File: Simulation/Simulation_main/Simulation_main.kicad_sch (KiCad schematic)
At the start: 13 parts, among them U1 ${SIM.PARAMS}, U2 ${SIM.PARAMS}

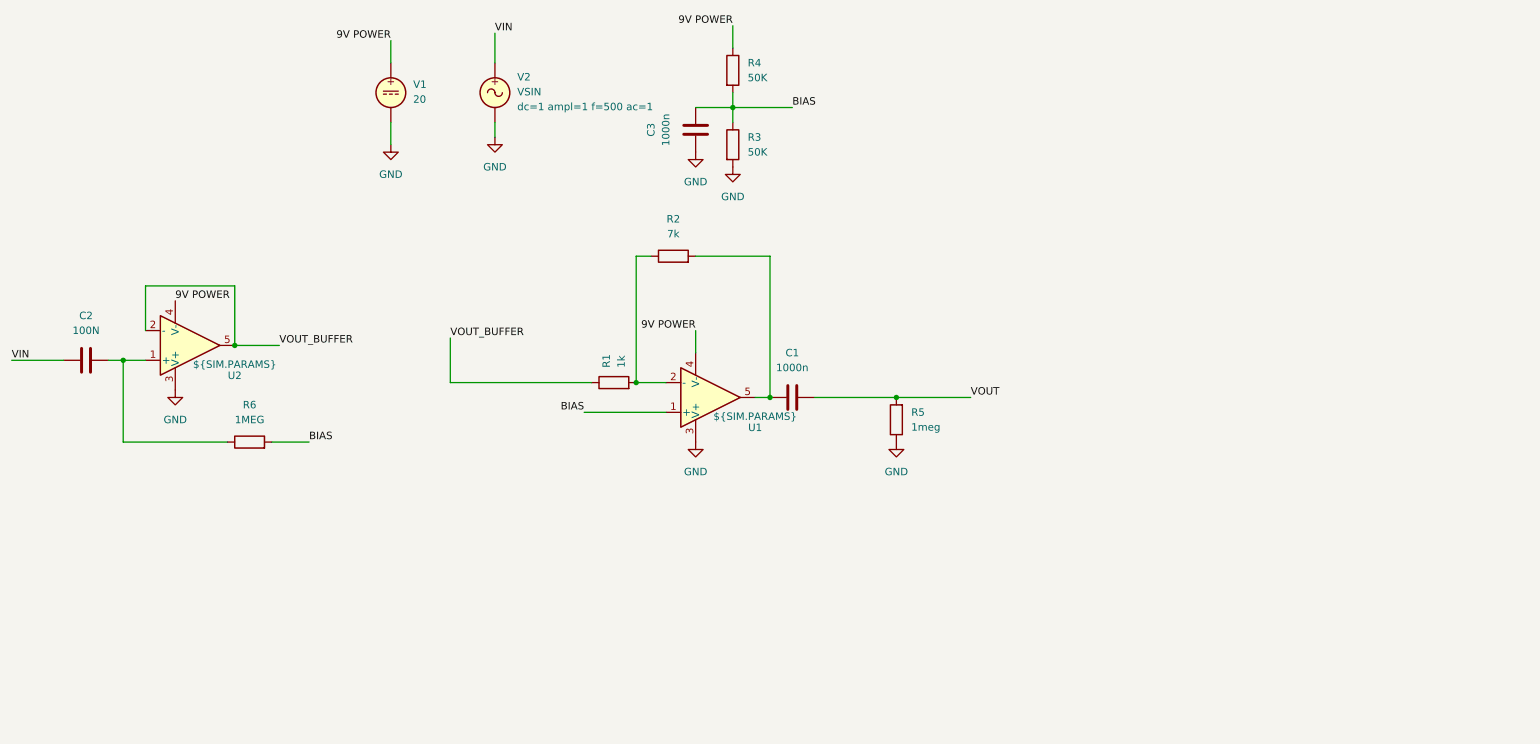
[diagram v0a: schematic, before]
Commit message: Dodany mikser do symulacji
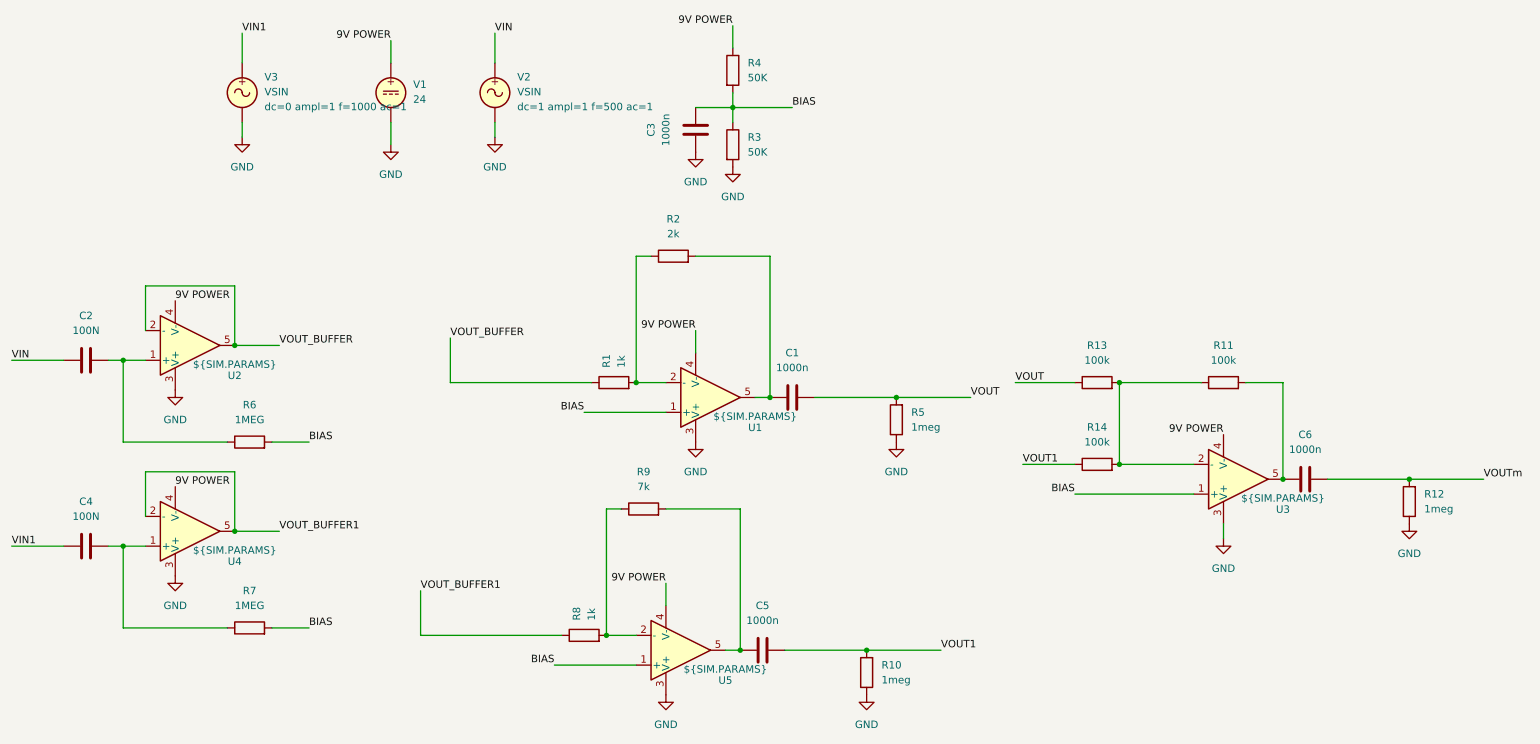
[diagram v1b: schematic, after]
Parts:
- added C4: 100N, symbol Device:C
- added C5, C6: 1000n, symbol Device:C
- added R10, R12: 1meg, symbol Device:R
- added R11, R13, R14: 100k, symbol Device:R
- added R7: 1MEG, symbol Device:R
- added R8: 1k, symbol Device:R
- added R9: 7k, symbol Device:R
- added U3, U4, U5: ${SIM.PARAMS}, symbol Simulation_SPICE:OPAMP
- added V3: VSIN, symbol Simulation_SPICE:VSIN
- R2: value 7k -> 2k
- V1: value 20 -> 24
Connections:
- net 9V POWER: now also U3.4 (V-), U4.4 (V-), U5.4 (V-)
- net BIAS: now also R7.2, U3.1 (+), U5.1 (+)
- net GND: now also R10.1, R12.1, U3.3 (V+), U4.3 (V+), U5.3 (V+), V3.2
- net VOUT: now also R13.1
- new net: R11.1, R13.2, R14.2, U3.2 (-)
- new net: C6.1, R11.2, U3.5
- new net: C4.2, R7.1, U4.1 (+)
- new net: R8.2, R9.1, U5.2 (-)
- new net: C5.1, R9.2, U5.5
- new net VIN1: C4.1, V3.1
- new net VOUT1: C5.2, R10.2, R14.1
- new net VOUT_BUFFER1: R8.1, U4.2 (-), U4.5
- new net VOUTm: C6.2, R12.2

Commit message: Dodanie schematicav1 oraz czesc footprintów
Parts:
- C1, C5: value 1000n -> 100n
- R4: value 50K -> 50k
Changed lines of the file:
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@@
 			)
 		)
-		(property "Value" "1000n"
+		(property "Value" "100n"
 			(at 157.48 86.36 90)
 			(effects
@@
 			)
 		)
-		(property "Value" "50K"
+		(property "Value" "50k"
 			(at 149.86 36.8299 0)
 			(effects
@@
 			)
 		)
-		(property "Value" "1000n"
+		(property "Value" "100n"
 			(at 152.4 129.54 90)
 			(effects
